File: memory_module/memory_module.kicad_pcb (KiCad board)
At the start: 2 copper layers, 100 x 100 mm, 93 parts, among them J1 Conn_01x06_Pin, J2 Conn_01x08_Pin, SW1 SW_DIP_x08, SW2 SW_DIP_x08, SW3 SW_DIP_x08, SW4 SW_DIP_x08, SW5 SW_DIP_x08, SW6 SW_DIP_x08, SW7 SW_DIP_x08, SW8 SW_DIP_x08, U1 74HC138, U2 74HC540

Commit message: ガーバーファイル作成
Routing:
- net Net-(D57-K): track 69.4 -> 38.9 mm, vias 0 -> 1
- net A0: track 84.0 -> 87.1 mm
- net +5V: track 151.2 -> 149.1 mm
- net Net-(D1-K): track 121.6 -> 123.5 mm
- net A1: track 86.4 -> 87.8 mm
- net Net-(U2-A0): track 278.9 -> 280.0 mm
- net Net-(U2-A4): track 293.2 -> 294.3 mm
- net Net-(U2-A3): track 288.6 -> 289.8 mm
- net Net-(U2-A2): track 285.2 -> 286.3 mm
- net Net-(U2-A1): track 282.0 -> 283.2 mm
- net Net-(D10-K): track 95.5 -> 96.3 mm
- net Net-(U2-A7): track 337.3 -> 336.7 mm
- net GND: track 154.9 -> 155.5 mm
- added copper zone on B.Cu, net GND
- added copper zone on F.Cu, net GND
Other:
- board text added: "TD4 Memory Module v1.0.0"

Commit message: wip
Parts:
- moved D68 80.2 mm to (117.5, 48.9)
- moved U1 71.7 mm to (47.6, 121.3), turned to 90 degrees
- moved D25 69.6 mm to (117.5, 70.5)
- moved D26 69.6 mm to (120.0, 70.5)
- moved D27 69.6 mm to (122.5, 70.5)
- moved D28 69.6 mm to (125.1, 70.5)
- moved D29 69.6 mm to (127.6, 70.5)
- moved D31 69.6 mm to (132.7, 70.5)
- moved D32 69.6 mm to (135.2, 70.5)
- moved SW4 69.6 mm to (117.5, 60.3)
- moved D30 69.6 mm to (130.2, 70.5)
- moved D71 55.7 mm to (93.3, 81.9)
- moved D72 51.6 mm to (117.5, 81.9)
- moved D49 44.4 mm to (93.3, 103.5)
- moved D51 44.4 mm to (98.4, 103.5)
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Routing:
- net GND: track 155.5 -> 0.00 mm
- net +5V: track 149.1 -> 0.00 mm
- net Net-(U2-A7): track 336.7 -> 214.8 mm
- net Net-(D1-K): track 123.5 -> 23.4 mm
- net Net-(U2-A6): track 304.0 -> 216.6 mm
- net Net-(U2-A5): track 299.2 -> 216.4 mm
- net Net-(U2-A4): track 294.3 -> 216.2 mm
- net Net-(D49-K): track 77.9 -> 0.00 mm, vias 1 -> 0
- net Net-(U2-A3): track 289.8 -> 216.2 mm
- net Net-(D10-K): track 96.3 -> 23.4 mm
- net Net-(U2-A2): track 286.3 -> 216.3 mm
- net Net-(D25-K): track 92.4 -> 23.4 mm, vias 1 -> 0
- net Net-(D33-K): track 69.0 -> 0.00 mm, vias 1 -> 0
- net Net-(U2-A1): track 283.2 -> 216.2 mm
- net Net-(U2-A0): track 280.0 -> 214.5 mm
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
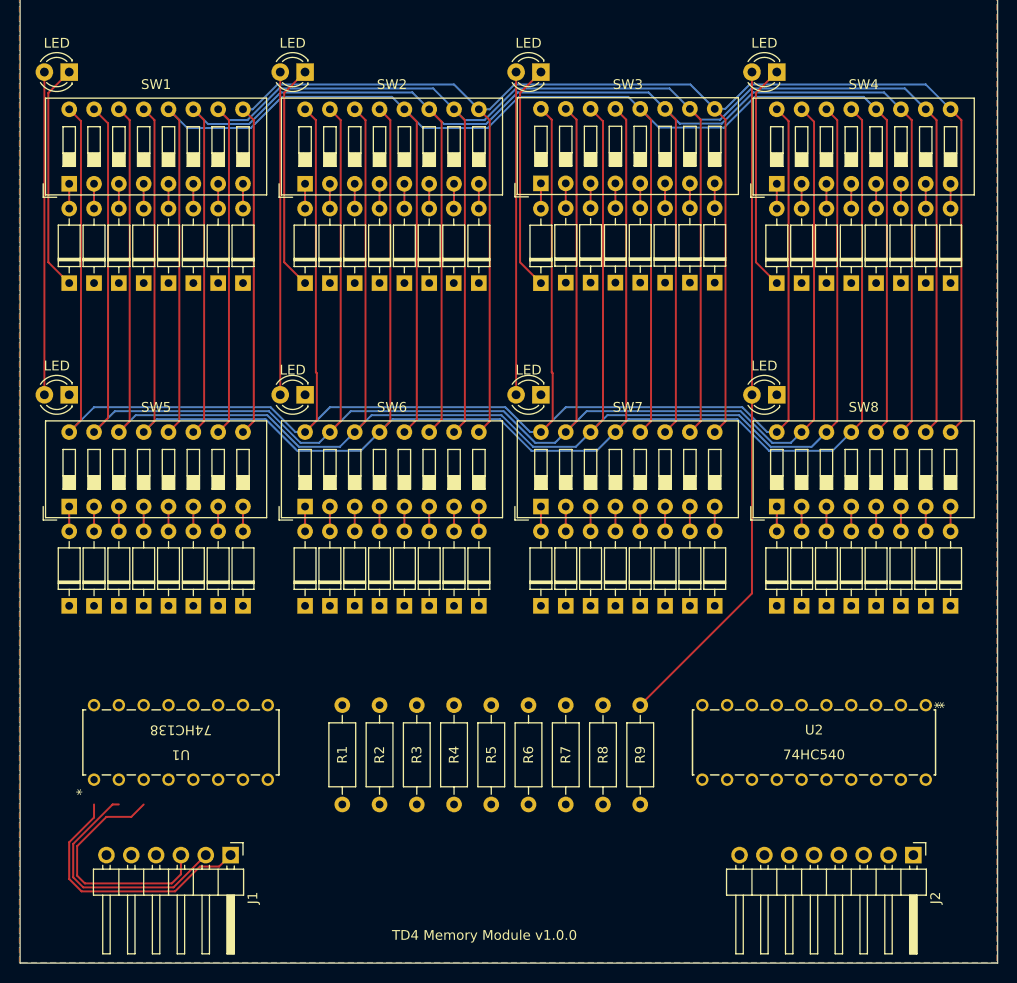
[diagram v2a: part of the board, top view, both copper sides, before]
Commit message: pcbをデザイン変更
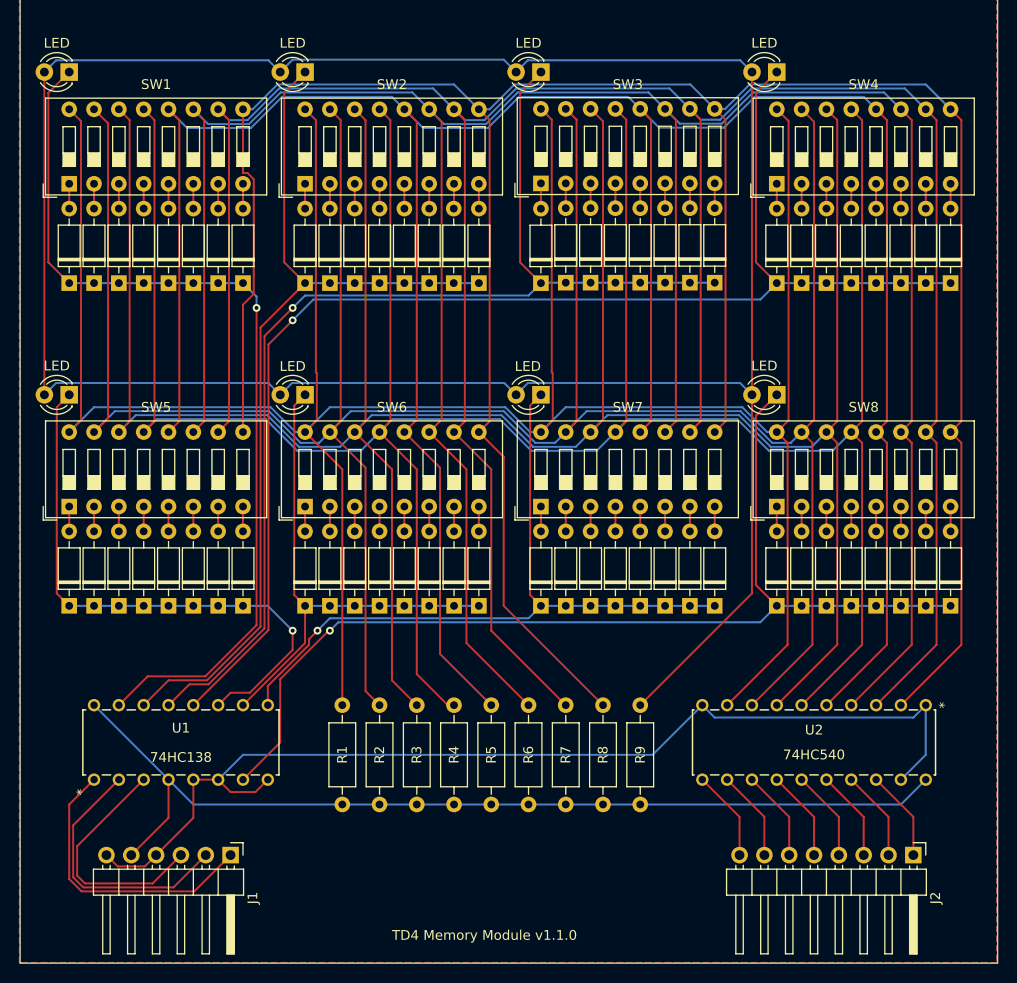
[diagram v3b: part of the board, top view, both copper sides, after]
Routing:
- net Net-(D25-K): track 23.4 -> 135.8 mm, vias 0 -> 1
- net GND: track 0.00 -> 109.3 mm
- net Net-(D57-K): track 0.00 -> 106.9 mm, vias 0 -> 1
- net +5V: track 0.00 -> 99.6 mm
- net Net-(D17-K): track 23.4 -> 114.7 mm, vias 0 -> 1
- net Net-(D65-A): track 168.6 -> 253.3 mm
- net Net-(D49-K): track 0.00 -> 73.9 mm, vias 0 -> 1
- net Net-(D1-K): track 23.4 -> 94.2 mm, vias 0 -> 1
- net Net-(D10-K): track 23.4 -> 93.5 mm
- net Net-(U2-A0): track 214.5 -> 278.9 mm
- net Net-(U2-A1): track 216.2 -> 279.8 mm
- net Net-(U2-A2): track 216.3 -> 279.4 mm
- net Net-(U2-A3): track 216.2 -> 278.8 mm
- net Net-(U2-A4): track 216.2 -> 278.6 mm
- net Net-(U2-A5): track 216.4 -> 277.9 mm
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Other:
- board text added: "TD4 Memory Module v1.1.0"
- board text removed: "TD4 Memory Module v1.0.0"

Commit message: wip
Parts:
- added D100: 1N4148, Diode_THT:D_DO-35_SOD27_P2.54mm_Vertical_KathodeUp, F.Cu at (-76.8, 114.9)
- added D101: 1N4148, Diode_THT:D_DO-35_SOD27_P2.54mm_Vertical_KathodeUp, F.Cu at (-74.3, 114.9)
- added D102: 1N4148, Diode_THT:D_DO-35_SOD27_P2.54mm_Vertical_KathodeUp, F.Cu at (-71.8, 114.9)
- added D103: 1N4148, Diode_THT:D_DO-35_SOD27_P2.54mm_Vertical_KathodeUp, F.Cu at (-69.2, 114.9)
- added D104: 1N4148, Diode_THT:D_DO-35_SOD27_P2.54mm_Vertical_KathodeUp, F.Cu at (-66.7, 114.9)
- added D105: 1N4148, Diode_THT:D_DO-35_SOD27_P2.54mm_Vertical_KathodeUp, F.Cu at (-60.3, 114.9)
- added D106: 1N4148, Diode_THT:D_DO-35_SOD27_P2.54mm_Vertical_KathodeUp, F.Cu at (-57.8, 114.9)
- added D107: 1N4148, Diode_THT:D_DO-35_SOD27_P2.54mm_Vertical_KathodeUp, F.Cu at (-55.2, 114.9)
- added D108: 1N4148, Diode_THT:D_DO-35_SOD27_P2.54mm_Vertical_KathodeUp, F.Cu at (-52.7, 114.9)
- added D109: 1N4148, Diode_THT:D_DO-35_SOD27_P2.54mm_Vertical_KathodeUp, F.Cu at (-50.2, 114.9)
- added D110: 1N4148, Diode_THT:D_DO-35_SOD27_P2.54mm_Vertical_KathodeUp, F.Cu at (-47.6, 114.9)
- added D111: 1N4148, Diode_THT:D_DO-35_SOD27_P2.54mm_Vertical_KathodeUp, F.Cu at (-45.1, 114.9)
- added D112: 1N4148, Diode_THT:D_DO-35_SOD27_P2.54mm_Vertical_KathodeUp, F.Cu at (-42.5, 114.9)
- added D113: 1N4148, Diode_THT:D_DO-35_SOD27_P2.54mm_Vertical_KathodeUp, F.Cu at (-36.2, 114.9)
- added D114: 1N4148, Diode_THT:D_DO-35_SOD27_P2.54mm_Vertical_KathodeUp, F.Cu at (-33.7, 114.9)
- added D115: 1N4148, Diode_THT:D_DO-35_SOD27_P2.54mm_Vertical_KathodeUp, F.Cu at (-31.1, 114.9)
- added D116: 1N4148, Diode_THT:D_DO-35_SOD27_P2.54mm_Vertical_KathodeUp, F.Cu at (-28.6, 114.9)
- added D117: 1N4148, Diode_THT:D_DO-35_SOD27_P2.54mm_Vertical_KathodeUp, F.Cu at (-26.0, 114.9)
- added D118: 1N4148, Diode_THT:D_DO-35_SOD27_P2.54mm_Vertical_KathodeUp, F.Cu at (-23.5, 114.9)
- added D119: 1N4148, Diode_THT:D_DO-35_SOD27_P2.54mm_Vertical_KathodeUp, F.Cu at (-21.0, 114.9)
- added D120: 1N4148, Diode_THT:D_DO-35_SOD27_P2.54mm_Vertical_KathodeUp, F.Cu at (-18.4, 114.9)
- added D121: 1N4148, Diode_THT:D_DO-35_SOD27_P2.54mm_Vertical_KathodeUp, F.Cu at (-12.1, 114.9)
- added D122: 1N4148, Diode_THT:D_DO-35_SOD27_P2.54mm_Vertical_KathodeUp, F.Cu at (-9.53, 114.9)
- added D123: 1N4148, Diode_THT:D_DO-35_SOD27_P2.54mm_Vertical_KathodeUp, F.Cu at (-6.99, 114.9)
- added D124: 1N4148, Diode_THT:D_DO-35_SOD27_P2.54mm_Vertical_KathodeUp, F.Cu at (-4.45, 114.9)
- added D125: 1N4148, Diode_THT:D_DO-35_SOD27_P2.54mm_Vertical_KathodeUp, F.Cu at (-1.91, 114.9)
- added D126: 1N4148, Diode_THT:D_DO-35_SOD27_P2.54mm_Vertical_KathodeUp, F.Cu at (0.63, 114.9)
- added D127: 1N4148, Diode_THT:D_DO-35_SOD27_P2.54mm_Vertical_KathodeUp, F.Cu at (3.17, 114.9)
- added D128: 1N4148, Diode_THT:D_DO-35_SOD27_P2.54mm_Vertical_KathodeUp, F.Cu at (5.71, 114.9)
- added D137: LED, LED_THT:LED_D3.0mm, F.Cu at (42.5, 88.3)
- added D138: LED, LED_THT:LED_D3.0mm, F.Cu at (66.7, 88.3)
- added D139: LED, LED_THT:LED_D3.0mm, F.Cu at (90.8, 88.3)
- added D140: LED, LED_THT:LED_D3.0mm, F.Cu at (114.9, 88.3)
- added D141: LED, LED_THT:LED_D3.0mm, F.Cu at (-17.1, 67.9)
- added D142: LED, LED_THT:LED_D3.0mm, F.Cu at (-10.6, 68.1)
- added D143: LED, LED_THT:LED_D3.0mm, F.Cu at (-5.72, 67.9)
- added D144: LED, LED_THT:LED_D3.0mm, F.Cu at (1.90, 68.1)
- added D65: 1N4148, Diode_THT:D_DO-35_SOD27_P2.54mm_Vertical_KathodeUp, F.Cu at (45.1, 106.0)
- added D66: 1N4148, Diode_THT:D_DO-35_SOD27_P2.54mm_Vertical_KathodeUp, F.Cu at (47.6, 106.0)
- added D67: 1N4148, Diode_THT:D_DO-35_SOD27_P2.54mm_Vertical_KathodeUp, F.Cu at (50.2, 106.0)
- added D68: 1N4148, Diode_THT:D_DO-35_SOD27_P2.54mm_Vertical_KathodeUp, F.Cu at (52.7, 106.0)
- added D69: 1N4148, Diode_THT:D_DO-35_SOD27_P2.54mm_Vertical_KathodeUp, F.Cu at (55.2, 106.0)
- added D70: 1N4148, Diode_THT:D_DO-35_SOD27_P2.54mm_Vertical_KathodeUp, F.Cu at (57.8, 106.0)
- added D71: 1N4148, Diode_THT:D_DO-35_SOD27_P2.54mm_Vertical_KathodeUp, F.Cu at (60.3, 106.0)
- added D72: 1N4148, Diode_THT:D_DO-35_SOD27_P2.54mm_Vertical_KathodeUp, F.Cu at (62.9, 106.0)
- added D73: 1N4148, Diode_THT:D_DO-35_SOD27_P2.54mm_Vertical_KathodeUp, F.Cu at (69.2, 106.0)
- added D74: 1N4148, Diode_THT:D_DO-35_SOD27_P2.54mm_Vertical_KathodeUp, F.Cu at (71.8, 106.0)
- added D75: 1N4148, Diode_THT:D_DO-35_SOD27_P2.54mm_Vertical_KathodeUp, F.Cu at (74.3, 106.0)
- added D76: 1N4148, Diode_THT:D_DO-35_SOD27_P2.54mm_Vertical_KathodeUp, F.Cu at (76.8, 106.0)
- added D77: 1N4148, Diode_THT:D_DO-35_SOD27_P2.54mm_Vertical_KathodeUp, F.Cu at (79.4, 106.0)
- added D78: 1N4148, Diode_THT:D_DO-35_SOD27_P2.54mm_Vertical_KathodeUp, F.Cu at (81.9, 106.0)
- added D79: 1N4148, Diode_THT:D_DO-35_SOD27_P2.54mm_Vertical_KathodeUp, F.Cu at (84.5, 106.0)
- added D80: 1N4148, Diode_THT:D_DO-35_SOD27_P2.54mm_Vertical_KathodeUp, F.Cu at (87.0, 106.0)
- added D81: 1N4148, Diode_THT:D_DO-35_SOD27_P2.54mm_Vertical_KathodeUp, F.Cu at (93.3, 106.0)
- added D82: 1N4148, Diode_THT:D_DO-35_SOD27_P2.54mm_Vertical_KathodeUp, F.Cu at (95.9, 106.0)
- added D83: 1N4148, Diode_THT:D_DO-35_SOD27_P2.54mm_Vertical_KathodeUp, F.Cu at (98.4, 106.0)
- added D84: 1N4148, Diode_THT:D_DO-35_SOD27_P2.54mm_Vertical_KathodeUp, F.Cu at (101.0, 106.0)
- added D85: 1N4148, Diode_THT:D_DO-35_SOD27_P2.54mm_Vertical_KathodeUp, F.Cu at (103.5, 106.0)
- added D86: 1N4148, Diode_THT:D_DO-35_SOD27_P2.54mm_Vertical_KathodeUp, F.Cu at (106.0, 106.0)
- added D87: 1N4148, Diode_THT:D_DO-35_SOD27_P2.54mm_Vertical_KathodeUp, F.Cu at (108.6, 106.0)
- added D88: 1N4148, Diode_THT:D_DO-35_SOD27_P2.54mm_Vertical_KathodeUp, F.Cu at (111.1, 106.0)
- added D89: 1N4148, Diode_THT:D_DO-35_SOD27_P2.54mm_Vertical_KathodeUp, F.Cu at (117.5, 106.0)
- added D90: 1N4148, Diode_THT:D_DO-35_SOD27_P2.54mm_Vertical_KathodeUp, F.Cu at (120.0, 106.0)
- added D91: 1N4148, Diode_THT:D_DO-35_SOD27_P2.54mm_Vertical_KathodeUp, F.Cu at (122.5, 106.0)
- added D92: 1N4148, Diode_THT:D_DO-35_SOD27_P2.54mm_Vertical_KathodeUp, F.Cu at (125.1, 106.0)
- added D93: 1N4148, Diode_THT:D_DO-35_SOD27_P2.54mm_Vertical_KathodeUp, F.Cu at (127.6, 106.0)
- added D94: 1N4148, Diode_THT:D_DO-35_SOD27_P2.54mm_Vertical_KathodeUp, F.Cu at (130.2, 106.0)
- added D95: 1N4148, Diode_THT:D_DO-35_SOD27_P2.54mm_Vertical_KathodeUp, F.Cu at (132.7, 106.0)
- added D96: 1N4148, Diode_THT:D_DO-35_SOD27_P2.54mm_Vertical_KathodeUp, F.Cu at (135.2, 106.0)
- added D97: 1N4148, Diode_THT:D_DO-35_SOD27_P2.54mm_Vertical_KathodeUp, F.Cu at (-84.5, 114.9)
- added D98: 1N4148, Diode_THT:D_DO-35_SOD27_P2.54mm_Vertical_KathodeUp, F.Cu at (-81.9, 114.9)
- added D99: 1N4148, Diode_THT:D_DO-35_SOD27_P2.54mm_Vertical_KathodeUp, F.Cu at (-79.4, 114.9)
- added SW10: SW_DIP_x08, Button_Switch_THT:SW_DIP_SPSTx08_Slide_9.78x22.5mm_W7.62mm_P2.54mm, F.Cu at (69.2, 99.7)
- added SW11: SW_DIP_x08, Button_Switch_THT:SW_DIP_SPSTx08_Slide_9.78x22.5mm_W7.62mm_P2.54mm, F.Cu at (93.3, 99.7)
- added SW12: SW_DIP_x08, Button_Switch_THT:SW_DIP_SPSTx08_Slide_9.78x22.5mm_W7.62mm_P2.54mm, F.Cu at (117.5, 99.7)
- added SW13: SW_DIP_x08, Button_Switch_THT:SW_DIP_SPSTx08_Slide_9.78x22.5mm_W7.62mm_P2.54mm, F.Cu at (-84.5, 108.6)
- added SW14: SW_DIP_x08, Button_Switch_THT:SW_DIP_SPSTx08_Slide_9.78x22.5mm_W7.62mm_P2.54mm, F.Cu at (-60.3, 108.6)
- added SW15: SW_DIP_x08, Button_Switch_THT:SW_DIP_SPSTx08_Slide_9.78x22.5mm_W7.62mm_P2.54mm, F.Cu at (-36.2, 108.6)
- added SW16: SW_DIP_x08, Button_Switch_THT:SW_DIP_SPSTx08_Slide_9.78x22.5mm_W7.62mm_P2.54mm, F.Cu at (-12.1, 108.6)
- added SW9: SW_DIP_x08, Button_Switch_THT:SW_DIP_SPSTx08_Slide_9.78x22.5mm_W7.62mm_P2.54mm, F.Cu at (45.1, 99.7)
- added U2: 74HC138, TD4_footprint:DIP16_TOS, F.Cu at (89.5, 135.2)
- D1, D10, D11, D12, D13, D14, D15, D16, D17, D18, D19, D2, D20, D21, D22, D23, D24, D25, D26, D27, D28, D29, D3, D30, D31, D32, D33, D34, D35, D36, D37, D38, D39, D4, D40, D41, D42, D43, D44, D45, D46, D47, D48, D49, D5, D50, D51, D52, D53, D54, D55, D56, D57, D58, D59, D6, D60, D61, D62, D63, D64, D7, D8, D9: footprint Diode_THT:D_DO-35_SOD27_P7.62mm_Horizontal -> Diode_THT:D_DO-35_SOD27_P2.54mm_Vertical_KathodeUp
- moved R1 94.9 mm to (164.5, 139.1)
- moved R2 94.9 mm to (168.3, 139.1)
- moved R3 94.9 mm to (172.1, 139.1)
- moved R6 94.9 mm to (183.5, 139.1)
- moved R7 94.9 mm to (187.3, 139.1)
- moved R8 94.9 mm to (191.1, 139.1)
- moved R9 94.9 mm to (194.9, 149.2)
- moved R4 94.9 mm to (175.9, 139.1)
- moved R5 94.9 mm to (179.7, 139.1)
- moved U1 24.7 mm to (67.9, 135.2)
- moved D33 20.3 mm to (45.1, 83.2)
- moved D34 20.3 mm to (47.6, 83.2)
- moved D35 20.3 mm to (50.2, 83.2)
- moved D36 20.3 mm to (52.7, 83.2)
- moved D37 20.3 mm to (55.2, 83.2)
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- renumbered D65 to D129, D66 to D130, D67 to D131, D68 to D132, D69 to D133, D70 to D134, D71 to D135, D72 to D136, U2 to U3
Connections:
- J1 pad 4: GND -> A3
- U1 pad 5: GND -> A3
- U1 pad 6: GND -> A3
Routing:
- net Net-(U3-A1): track 279.8 -> 0.00 mm
- net Net-(U3-A2): track 279.4 -> 0.00 mm
- net Net-(U3-A0): track 278.9 -> 0.00 mm
- net Net-(U3-A3): track 278.8 -> 0.00 mm
- net Net-(U3-A4): track 278.6 -> 0.00 mm
- net Net-(U3-A5): track 277.9 -> 0.00 mm
- net Net-(U3-A6): track 277.6 -> 0.00 mm
- net Net-(U3-A7): track 275.3 -> 0.00 mm
- net Net-(D129-A): track 253.3 -> 0.00 mm
- net Net-(D132-K): track 135.8 -> 0.00 mm, vias 1 -> 0
- net Net-(D131-K): track 114.7 -> 0.00 mm, vias 1 -> 0
- net GND: track 109.3 -> 0.00 mm
- net Net-(D136-K): track 106.9 -> 0.00 mm, vias 1 -> 0
- net +5V: track 99.6 -> 0.00 mm
- net Net-(D1-K): track 94.2 -> 0.00 mm, vias 1 -> 0
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
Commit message: wip
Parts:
- removed D129, D130, D131, D132, D133, D134, D135, D136, D137, D138, D139, D140, D141, D142, D143, D144: LED, LED_THT:LED_D3.0mm
- removed R9: R, Resistor_THT:R_Axial_DIN0207_L6.3mm_D2.5mm_P10.16mm_Horizontal
- moved D100 129.3 mm to (52.5, 118.3)
- moved D102 129.3 mm to (57.5, 118.3)
- moved D104 129.3 mm to (62.6, 118.3)
- moved D107 129.3 mm to (74.0, 118.3)
- moved D109 129.3 mm to (79.1, 118.3)
- moved D111 129.3 mm to (84.2, 118.3)
- moved D113 129.3 mm to (93.1, 118.3)
- moved D118 129.3 mm to (105.8, 118.3)
- moved D120 129.3 mm to (110.9, 118.3)
- moved D127 129.3 mm to (132.5, 118.3)
- moved SW15 129.3 mm to (93.1, 112.0)
- moved D101 129.3 mm to (55.0, 118.3)
- moved D103 129.3 mm to (60.1, 118.3)
- moved D105 129.3 mm to (69.0, 118.3)
- moved D106 129.3 mm to (71.5, 118.3)
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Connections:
- U2 pad 10: Net-(D142-K) -> Net-(D105-K)
- U2 pad 11: Net-(D141-K) -> Net-(D100-K)
- U2 pad 12: Net-(D140-K) -> Net-(D89-K)
- U2 pad 13: Net-(D139-K) -> Net-(D81-K)
- U2 pad 14: Net-(D138-K) -> Net-(D73-K)
- U2 pad 15: Net-(D137-K) -> Net-(D65-K)
- U2 pad 7: Net-(D144-K) -> Net-(D121-K)
- U2 pad 9: Net-(D143-K) -> Net-(D113-K)
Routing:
- removed copper zone on B.Cu, net GND
- removed copper zone on F.Cu, net GND

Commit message: とりあえず配線した、美しくはない
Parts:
- added D129: LED, LED_SMD:LED_1206_3216Metric_Pad1.42x1.75mm_HandSolder, F.Cu at (43.8, 55.9)
- added D130: LED, LED_SMD:LED_1206_3216Metric_Pad1.42x1.75mm_HandSolder, F.Cu at (67.9, 55.9)
- added D131: LED, LED_SMD:LED_1206_3216Metric_Pad1.42x1.75mm_HandSolder, F.Cu at (92.1, 55.9)
- added D132: LED, LED_SMD:LED_1206_3216Metric_Pad1.42x1.75mm_HandSolder, F.Cu at (116.1, 55.7)
- added D133: LED, LED_SMD:LED_1206_3216Metric_Pad1.42x1.75mm_HandSolder, F.Cu at (43.8, 76.2)
- added D134: LED, LED_SMD:LED_1206_3216Metric_Pad1.42x1.75mm_HandSolder, F.Cu at (67.9, 76.2)
- added D135: LED, LED_SMD:LED_1206_3216Metric_Pad1.42x1.75mm_HandSolder, F.Cu at (92.1, 76.2)
- added D136: LED, LED_SMD:LED_1206_3216Metric_Pad1.42x1.75mm_HandSolder, F.Cu at (116.2, 76.2)
- added D137: LED, LED_SMD:LED_1206_3216Metric_Pad1.42x1.75mm_HandSolder, F.Cu at (43.8, 96.5)
- added D138: LED, LED_SMD:LED_1206_3216Metric_Pad1.42x1.75mm_HandSolder, F.Cu at (67.9, 96.5)
- added D139: LED, LED_SMD:LED_1206_3216Metric_Pad1.42x1.75mm_HandSolder, F.Cu at (92.1, 96.5)
- added D140: LED, LED_SMD:LED_1206_3216Metric_Pad1.42x1.75mm_HandSolder, F.Cu at (116.2, 96.5)
- added D141: LED, LED_SMD:LED_1206_3216Metric_Pad1.42x1.75mm_HandSolder, F.Cu at (43.8, 117.1)
- added D142: LED, LED_SMD:LED_1206_3216Metric_Pad1.42x1.75mm_HandSolder, F.Cu at (67.9, 116.8)
- added D143: LED, LED_SMD:LED_1206_3216Metric_Pad1.42x1.75mm_HandSolder, F.Cu at (92.1, 116.8)
- added D144: LED, LED_SMD:LED_1206_3216Metric_Pad1.42x1.75mm_HandSolder, F.Cu at (116.2, 116.8)
- added R9: 1K, Resistor_THT:R_Axial_DIN0207_L6.3mm_D2.5mm_P2.54mm_Vertical, F.Cu at (109.8, 134.0)
- R1, R2: value R -> 10K; footprint Resistor_THT:R_Axial_DIN0207_L6.3mm_D2.5mm_P10.16mm_Horizontal -> Resistor_THT:R_Axial_DIN0207_L6.3mm_D2.5mm_P2.54mm_Vertical
- R3, R4, R5, R6, R7, R8: footprint Resistor_THT:R_Axial_DIN0207_L6.3mm_D2.5mm_P10.16mm_Horizontal -> Resistor_THT:R_Axial_DIN0207_L6.3mm_D2.5mm_P2.54mm_Vertical
- moved R1 4.03 mm to (87.6, 127.2)
- moved R2 4.03 mm to (90.8, 127.2)
- moved R3 4.03 mm to (94.0, 127.2)
- moved R4 4.03 mm to (97.2, 127.2)
- moved R5 4.03 mm to (100.3, 127.2)
- moved R6 4.03 mm to (103.5, 127.2)
- moved R7 4.03 mm to (106.7, 127.2)
- moved R8 4.03 mm to (109.8, 127.2)
- moved D73 1.62 mm to (70.5, 97.8)
- moved D78 1.62 mm to (83.2, 97.8)
- moved D80 1.62 mm to (88.3, 97.8)
- moved D82 1.62 mm to (97.2, 97.8)
- moved D84 1.62 mm to (102.2, 97.8)
- moved D93 1.62 mm to (128.9, 97.8)
- moved D94 1.62 mm to (131.4, 97.8)
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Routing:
- net Net-(U3-A7): track 0.00 -> 393.6 mm
- net Net-(U3-A6): track 0.00 -> 392.8 mm
- net Net-(U3-A4): track 0.00 -> 392.3 mm
- net Net-(U3-A5): track 0.00 -> 391.8 mm
- net Net-(U3-A3): track 0.00 -> 391.4 mm
- net Net-(U3-A2): track 0.00 -> 391.2 mm
- net Net-(U3-A1): track 0.00 -> 390.9 mm
- net Net-(U3-A0): track 0.00 -> 390.4 mm
- net Net-(D129-A): track 0.00 -> 362.2 mm, vias 0 -> 4
- net Net-(D132-K): track 0.00 -> 169.1 mm, vias 0 -> 2
- net Net-(D131-K): track 0.00 -> 143.6 mm, vias 0 -> 2
- net GND: track 0.00 -> 142.0 mm
- net Net-(D136-K): track 0.00 -> 122.9 mm, vias 0 -> 2
- net Net-(D10-K): track 0.00 -> 118.2 mm, vias 0 -> 2
- net +5V: track 0.00 -> 115.0 mm
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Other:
- board text added: "5V"
- board text added: "A0"
- board text added: "A1"
- board text added: "A2"
- board text added: "A3"
- board text added: "D0"
- board text added: "D1"
- board text added: "D2"
- board text added: "D3"
- board text added: "D4"
- board text added: "D5"
- board text added: "D6"
- board text added: "D7"
- board text added: "GND"
- board text added: "TD4 Memory Module v1.2.0"
- board text removed: "TD4 Memory Module v1.1.0"

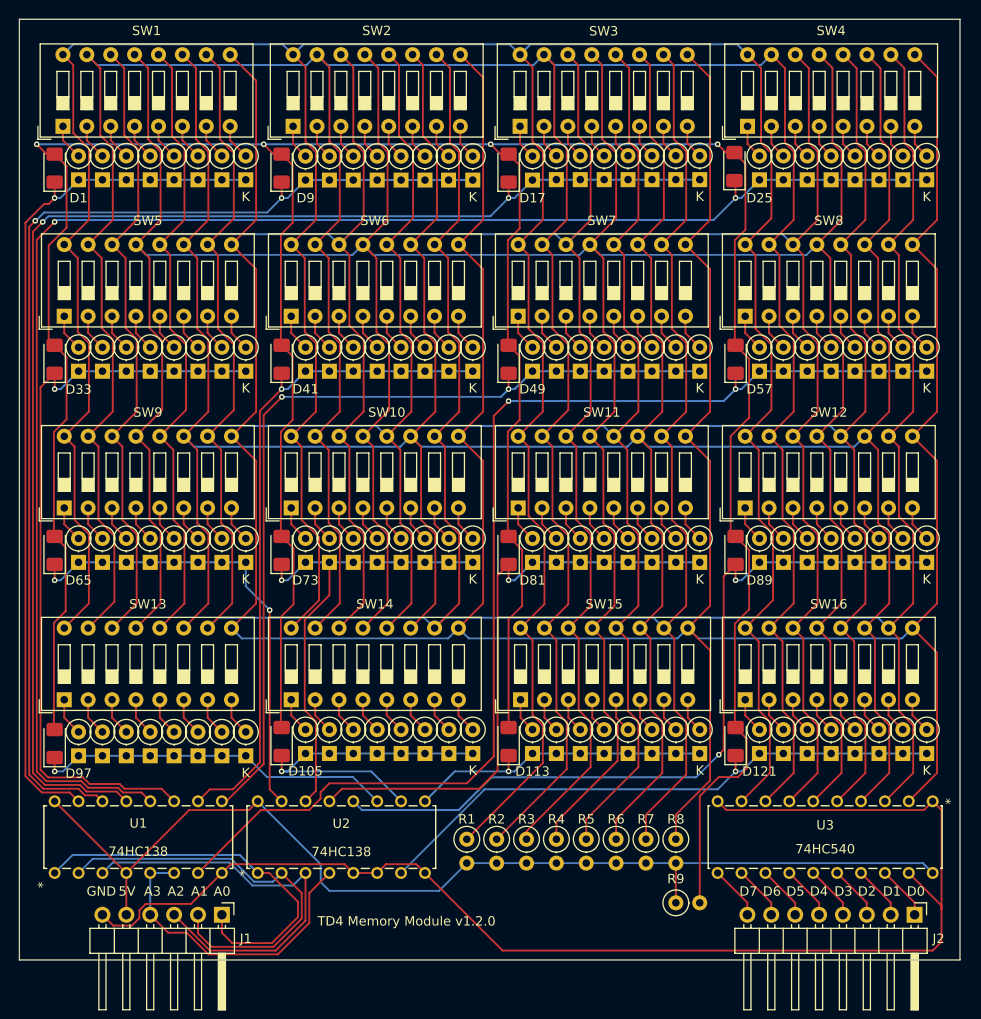
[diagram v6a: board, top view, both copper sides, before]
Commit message: 74HC138Nのenableを修正
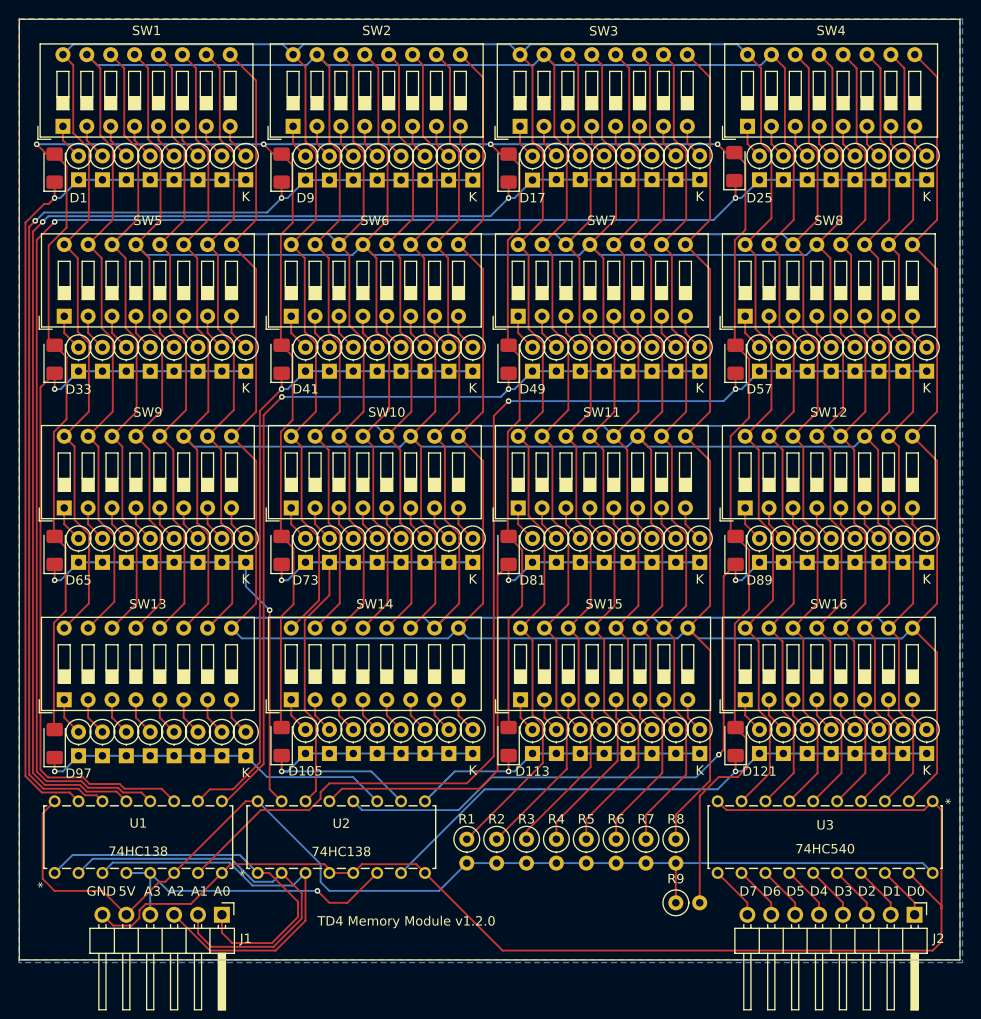
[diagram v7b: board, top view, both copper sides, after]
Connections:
- U1 pad 4: +5V -> A3
- U1 pad 6: A3 -> +5V
- U2 pad 4: A3 -> GND
- U2 pad 6: GND -> A3
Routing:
- net +5V: track 115.0 -> 120.9 mm
- net A3: track 33.2 -> 33.7 mm, vias 0 -> 1
- added copper zone on B.Cu, net GND
- added copper zone on F.Cu, net GND
